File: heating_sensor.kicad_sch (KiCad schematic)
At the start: 3 parts

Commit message: all unit test pass
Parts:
- C25: value 100nF -> 100n
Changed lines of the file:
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@@
 			)
 		)
-		(property "Value" "100nF"
+		(property "Value" "100n"
 			(at 18.415 15.24 0.0000)
 			(effects
@@
 		(instances
 			(project "Untitled"
-				(path "/2b46367b-7f7a-4d0b-a981-14ef6f17f746"
+				(path "/ce240599-ae42-4376-828a-09a891a5e9c6"
 					(reference "C25")
 					(unit 1)
@@
 		(instances
 			(project "Untitled"
-				(path "/2b46367b-7f7a-4d0b-a981-14ef6f17f746"
+				(path "/ce240599-ae42-4376-828a-09a891a5e9c6"
 					(reference "R25")
 					(unit 1)
@@
 		(instances
 			(project "Untitled"
-				(path "/2b46367b-7f7a-4d0b-a981-14ef6f17f746"
+				(path "/ce240599-ae42-4376-828a-09a891a5e9c6"
 					(reference "R26")
 					(unit 1)

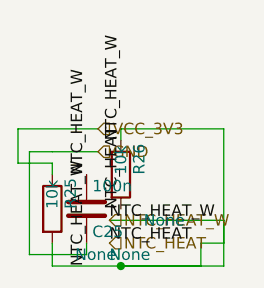
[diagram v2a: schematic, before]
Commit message: optimazed load to kicad
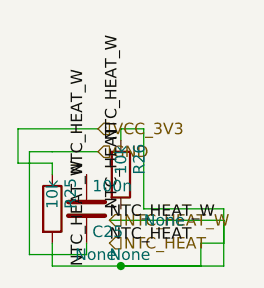
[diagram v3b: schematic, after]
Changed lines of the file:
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@@
 		(instances
 			(project "Untitled"
-				(path "/0573250a-45d1-4eb9-a46d-861c7a8e306a"
+				(path "/7edcb6ac-6215-4f27-8410-70bd096f4d3f"
 					(reference "C25")
 					(unit 1)
@@
 		(instances
 			(project "Untitled"
-				(path "/0573250a-45d1-4eb9-a46d-861c7a8e306a"
+				(path "/7edcb6ac-6215-4f27-8410-70bd096f4d3f"
 					(reference "R25")
 					(unit 1)
@@
 		(instances
 			(project "Untitled"
-				(path "/0573250a-45d1-4eb9-a46d-861c7a8e306a"
+				(path "/7edcb6ac-6215-4f27-8410-70bd096f4d3f"
 					(reference "R26")
 					(unit 1)
@@
 	(wire
 		(pts
-			(xy 21.59 8.89) (xy 33.02 8.89)
-		)
-		(stroke
-			(width 0)
-			(type default)
-		)
-	)
-	(wire
-		(pts
-			(xy 33.02 8.89) (xy 33.02 21.59)
-		)
-		(stroke
+			(xy 21.59 8.89) (xy 24.13 8.89)
+		)
+		(stroke
+			(width 0)
+			(type default)
+		)
+	)
+	(wire
+		(pts
+			(xy 24.13 8.89) (xy 24.13 17.78)
+		)
+		(stroke
+			(width 0)
+			(type default)
+		)
+	)
+	(wire
+		(pts
+			(xy 24.13 17.78) (xy 33.02 17.78)
+		)
+		(stroke
+			(width 0)
+			(type default)
+		)
+	)
+	(wire
+		(pts
+			(xy 33.02 17.78) (xy 33.02 21.59)
+		)
+		(stroke

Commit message: tests_fix
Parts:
- C25, R25, R26: hierarchy_path (none) -> /c5a034c1-1f54-4e7e-8711-0930d2b4314e/cce2be15-aa78-4c7e-aa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
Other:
- title: (none) -> climate_control_niva_travel
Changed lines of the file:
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@@
 	(generator_version "9.0")
 	(paper "A4")
+	(title_block
+		(title "climate_control_niva_travel")
+	)
 	(symbol
 		(lib_id "Device:C")
@@
 			)
 		)
+		(property "hierarchy_path" "/c5a034c1-1f54-4e7e-8711-0930d2b4314e/cce2be15-aa78-4c7e-aaa1-83c397742fef"
+			(at 20.32 22.8599 0)
+			(effects
+				(font
+					(size 1.27 1.27)
+				)
+				(justify left)
+			)
+		)
 		(pin "1"
 		)
@@
 		)
 		(instances
-			(project "Untitled"
-				(path "/7edcb6ac-6215-4f27-8410-70bd096f4d3f"
+			(project "climate_control_niva_travel"
+				(path "/c5a034c1-1f54-4e7e-8711-0930d2b4314e/cce2be15-aa78-4c7e-aaa1-83c397742fef"
 					(reference "C25")
 					(unit 1)
@@
 			)
 		)
+		(property "hierarchy_path" "/c5a034c1-1f54-4e7e-8711-0930d2b4314e/cce2be15-aa78-4c7e-aaa1-83c397742fef"
+			(at 16.51 22.8599 0)
+			(effects
+				(font
+					(size 1.27 1.27)
+				)
+				(justify left)
+			)
+		)
 		(pin "1"
 		)
@@
 		)
 		(instances
-			(project "Untitled"
-				(path "/7edcb6ac-6215-4f27-8410-70bd096f4d3f"
-					(reference "R25")
+			(project "climate_control_niva_travel"
+				(path "/c5a034c1-1f54-4e7e-8711-0930d2b4314e/cce2be15-aa78-4c7e-aaa1-83c397742fef"
+					(reference "R41")
 					(unit 1)
 				)
@@
 			)
 		)
+		(property "hierarchy_path" "/c5a034c1-1f54-4e7e-8711-0930d2b4314e/cce2be15-aa78-4c7e-aaa1-83c397742fef"
+			(at 24.13 19.0499 0)
+			(effects
+				(font
+					(size 1.27 1.27)
+				)
+				(justify left)
+			)
+		)
 		(pin "1"
 		)
@@
 		)
 		(instances
-			(project "Untitled"
-				(path "/7edcb6ac-6215-4f27-8410-70bd096f4d3f"
-					(reference "R26")
+			(project "climate_control_niva_travel"
+				(path "/c5a034c1-1f54-4e7e-8711-0930d2b4314e/cce2be15-aa78-4c7e-aaa1-83c397742fef"
+					(reference "R42")
 					(unit 1)
 				)
@@
 			(type default)
 		)
+	)
+	(junction
+		(at 17.78 24.13)
+		(diameter 0)
+		(color 0 0 0 0)
 	)
 	(junction
@@
 	)
 	(hierarchical_label "NTC_HEAT_W"
-		(shape input)
+		(shape output)
 		(at 20.32 19.05 0)
 		(effects
@@
 	)
 	(hierarchical_label "NTC_HEAT"
-		(shape input)
+		(shape output)
 		(at 20.32 21.59 0)
 		(effects

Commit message: refactoring
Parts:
- C25, R25, R26: hierarchy_path /c5a034c1-1f54-4e7e-8711-0930d2b4314e/cce2be15-aa78-4c7e-aa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 -> (none)
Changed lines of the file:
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@@
-			)
-		)
-		(property "hierarchy_path" "/c5a034c1-1f54-4e7e-8711-0930d2b4314e/cce2be15-aa78-4c7e-aaa1-83c397742fef"
-			(at 20.32 22.8599 0)
-			(effects
-				(font
-					(size 1.27 1.27)
-				)
-				(justify left)
 			)
 		)
@@
 		(instances
 			(project "climate_control_niva_travel"
-				(path "/c5a034c1-1f54-4e7e-8711-0930d2b4314e/cce2be15-aa78-4c7e-aaa1-83c397742fef"
-					(reference "C25")
+				(path "/165a98f1-2dde-4141-9fdc-c935d39c8cff/2827009f-f2b8-443b-9f5b-0ad26ce039e9/"
+					(reference "C0425")
 					(unit 1)
 				)
@@
 			)
 		)
-		(property "hierarchy_path" "/c5a034c1-1f54-4e7e-8711-0930d2b4314e/cce2be15-aa78-4c7e-aaa1-83c397742fef"
-			(at 16.51 22.8599 0)
-			(effects
-				(font
-					(size 1.27 1.27)
-				)
-				(justify left)
-			)
-		)
 		(pin "1"
 		)
@@
 		(instances
 			(project "climate_control_niva_travel"
-				(path "/c5a034c1-1f54-4e7e-8711-0930d2b4314e/cce2be15-aa78-4c7e-aaa1-83c397742fef"
-					(reference "R41")
+				(path "/165a98f1-2dde-4141-9fdc-c935d39c8cff/2827009f-f2b8-443b-9f5b-0ad26ce039e9/"
+					(reference "R0425")
 					(unit 1)
 				)
@@
 			)
 		)
-		(property "hierarchy_path" "/c5a034c1-1f54-4e7e-8711-0930d2b4314e/cce2be15-aa78-4c7e-aaa1-83c397742fef"
-			(at 24.13 19.0499 0)
-			(effects
-				(font
-					(size 1.27 1.27)
-				)
-				(justify left)
-			)
-		)
 		(pin "1"
 		)
@@
 		(instances
 			(project "climate_control_niva_travel"
-				(path "/c5a034c1-1f54-4e7e-8711-0930d2b4314e/cce2be15-aa78-4c7e-aaa1-83c397742fef"
-					(reference "R42")
+				(path "/165a98f1-2dde-4141-9fdc-c935d39c8cff/2827009f-f2b8-443b-9f5b-0ad26ce039e9/"
+					(reference "R0426")
 					(unit 1)
 				)

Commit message: refactoring
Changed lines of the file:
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@@
+			)
+		)
+		(property "Sim.Device" "C"
+			(at 20.32 22.8599 0)
+			(effects
+				(font
+					(size 1.27 1.27)
+				)
+				(justify left)
+			)
+		)
+		(property "Sim.Params" "C=100n"
+			(at 20.32 22.8599 0)
+			(effects
+				(font
+					(size 1.27 1.27)
+				)
+				(justify left)
 			)
 		)
@@
 		(instances
 			(project "climate_control_niva_travel"
-				(path "/165a98f1-2dde-4141-9fdc-c935d39c8cff/2827009f-f2b8-443b-9f5b-0ad26ce039e9/"
+				(path "/cc416b40-1361-4232-ac1e-5cd36ef0c0fb/4058bf07-d3ed-47ea-a155-e5643b2095d0/"
 					(reference "C0425")
 					(unit 1)
@@
 			)
 		)
+		(property "Sim.Device" "R"
+			(at 16.51 22.8599 0)
+			(effects
+				(font
+					(size 1.27 1.27)
+				)
+				(justify left)
+			)
+		)
+		(property "Sim.Params" "R=10k"
+			(at 16.51 22.8599 0)
+			(effects
+				(font
+					(size 1.27 1.27)
+				)
+				(justify left)
+			)
+		)
 		(pin "1"
 		)
@@
 		(instances
 			(project "climate_control_niva_travel"
-				(path "/165a98f1-2dde-4141-9fdc-c935d39c8cff/2827009f-f2b8-443b-9f5b-0ad26ce039e9/"
+				(path "/cc416b40-1361-4232-ac1e-5cd36ef0c0fb/4058bf07-d3ed-47ea-a155-e5643b2095d0/"
 					(reference "R0425")
 					(unit 1)
@@
 			)
 		)
+		(property "Sim.Device" "R"
+			(at 24.13 19.0499 0)
+			(effects
+				(font
+					(size 1.27 1.27)
+				)
+				(justify left)
+			)
+		)
+		(property "Sim.Params" "R=10k"
+			(at 24.13 19.0499 0)
+			(effects
+				(font
+					(size 1.27 1.27)
+				)
+				(justify left)
+			)
+		)
 		(pin "1"
 		)
@@
 		(instances
 			(project "climate_control_niva_travel"
-				(path "/165a98f1-2dde-4141-9fdc-c935d39c8cff/2827009f-f2b8-443b-9f5b-0ad26ce039e9/"
+				(path "/cc416b40-1361-4232-ac1e-5cd36ef0c0fb/4058bf07-d3ed-47ea-a155-e5643b2095d0/"
 					(reference "R0426")
 					(unit 1)
@@
 	(junction
 		(at 17.78 24.13)
-		(diameter 0)
+		(diameter 0.0000)
 		(color 0 0 0 0)
 	)
 	(junction
 		(at 21.59 24.13)
-		(diameter 0)
+		(diameter 0.0000)
 		(color 0 0 0 0)
 	)
@@
 		(effects
 			(font
-				(size 1.27 1.27)
-			)
-			(justify left bottom)
-		)
-	)
-	(label "NTC_HEAT_W"
-		(at 17.78 24.13 90)
-		(effects
-			(font
